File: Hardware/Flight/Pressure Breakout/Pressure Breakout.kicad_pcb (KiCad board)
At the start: 2 copper layers, 14 x 8.6 mm, 4 parts, among them J1 Conn_01x03, U1 ABPDANT005PGAA5

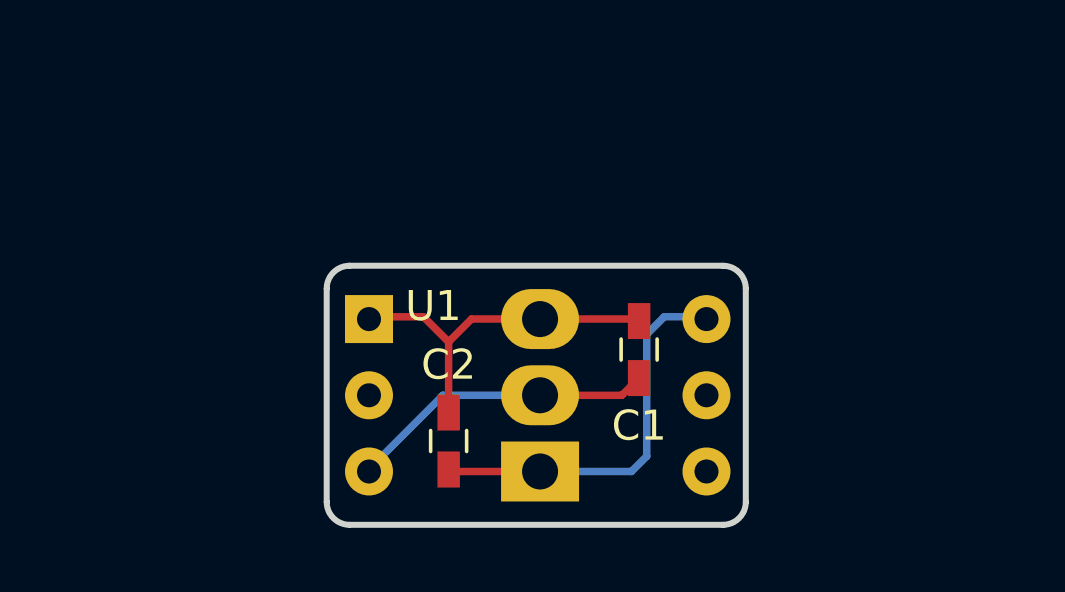
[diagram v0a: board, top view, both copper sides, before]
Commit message: updated pressure breakout
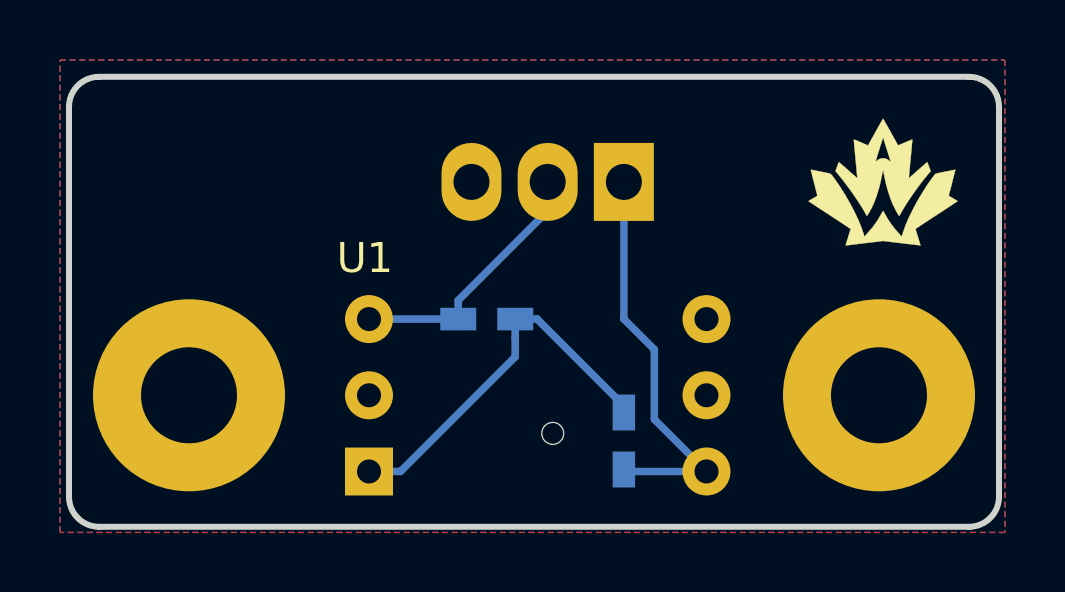
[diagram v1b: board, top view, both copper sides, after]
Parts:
- added G***: LOGO, Team_Logo:Logo_SilkScreen_5mm, B.Cu at (144.3, 95.5)
- added G***: LOGO, Team_Logo:Logo_SilkScreen_5mm, F.Cu at (167.1, 95.5)
- added REF**: MountingHole_3.2mm_M3_Pad, Mounting_Holes:MountingHole_3.2mm_M3_Pad, F.Cu at (144.0, 102.6)
- added REF**: MountingHole_3.2mm_M3_Pad, Mounting_Holes:MountingHole_3.2mm_M3_Pad, F.Cu at (167.0, 102.6)
- C1, C2: moved to B.Cu
- moved J1 10.0 mm to (158.5, 95.5), turned to 180 degrees
- moved C2 5.84 mm to (158.5, 104.1)
- moved C1 5.18 mm to (153.9, 100.1), turned to 0 degrees
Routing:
- net /VOUT: track 10.3 -> 9.18 mm
- net +5V: track 13.1 -> 14.1 mm
- net GND: track 12.0 -> 12.8 mm
- added copper zone on B.Cu, net GND
- added copper zone on F.Cu, net GND
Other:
- board size 14 x 8.6 mm -> 31 x 15 mm
- board text added: "1"
- board text added: "3"
